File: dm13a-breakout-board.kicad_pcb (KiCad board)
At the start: 2 copper layers, 50 x 50 mm, 11 parts, among them J1 Conn_01x02, J2 Conn_01x05, J3 Conn_01x08, J4 Conn_01x08, U1 DM13A

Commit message: Use different connector, add gnd pins, add silkscreen
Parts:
- J3, J4: value Conn_01x08 -> Conn_02x08_Odd_Even; footprint Connector_PinHeader_2.54mm:PinHeader_1x08_P2.54mm_Vertical -> Connector_PinSocket_2.54mm:PinSocket_2x08_P2.54mm_Vertical
- moved J4 2.50 mm to (89.5, 71.0)
- moved J3 0.55 mm to (63.5, 71.0)
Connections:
- net Net-(J3-Pin_1) renamed /0
- J3 pad 2: Net-(J3-Pin_2) -> GND
- J3 pad 3: Net-(J3-Pin_3) -> /1
- J3 pad 4: Net-(J3-Pin_4) -> GND
- J3 pad 5: Net-(J3-Pin_5) -> /2
- J3 pad 6: Net-(J3-Pin_6) -> GND
- J3 pad 7: Net-(J3-Pin_7) -> /3
- J3 pad 8: Net-(J3-Pin_8) -> GND
- J4 pad 1: Net-(J4-Pin_1) -> GND
- J4 pad 2: Net-(J4-Pin_2) -> /15
- J4 pad 3: Net-(J4-Pin_3) -> GND
- J4 pad 4: Net-(J4-Pin_4) -> /14
- J4 pad 5: Net-(J4-Pin_5) -> GND
- J4 pad 6: Net-(J4-Pin_6) -> /13
- J4 pad 7: Net-(J4-Pin_7) -> GND
- J4 pad 8: Net-(J4-Pin_8) -> /12
- U1 pad 10: Net-(J3-Pin_6) -> /5
- U1 pad 11: Net-(J3-Pin_7) -> /6
- U1 pad 12: Net-(J3-Pin_8) -> /7
- U1 pad 13: Net-(J4-Pin_8) -> /8
- U1 pad 14: Net-(J4-Pin_7) -> /9
- U1 pad 15: Net-(J4-Pin_6) -> /10
- U1 pad 16: Net-(J4-Pin_5) -> /11
- U1 pad 17: Net-(J4-Pin_4) -> /12
- U1 pad 18: Net-(J4-Pin_3) -> /13
- U1 pad 19: Net-(J4-Pin_2) -> /14
- U1 pad 20: Net-(J4-Pin_1) -> /15
- U1 pad 6: Net-(J3-Pin_2) -> /1
- U1 pad 7: Net-(J3-Pin_3) -> /2
- U1 pad 8: Net-(J3-Pin_4) -> /3
- U1 pad 9: Net-(J3-Pin_5) -> /4
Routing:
- net Net-(J4-Pin_2): track 8.53 -> 0.00 mm
- net /14: track 0.00 -> 8.53 mm
- net Net-(J4-Pin_8): track 8.53 -> 0.00 mm
- net Net-(J4-Pin_7): track 8.53 -> 0.00 mm
- net Net-(J4-Pin_6): track 8.53 -> 0.00 mm
- net Net-(J4-Pin_5): track 8.53 -> 0.00 mm
- net Net-(J4-Pin_4): track 8.53 -> 0.00 mm
- net Net-(J4-Pin_3): track 8.53 -> 0.00 mm
- net Net-(J4-Pin_1): track 8.53 -> 0.00 mm
- net /9: track 0.00 -> 8.53 mm
- net /8: track 0.00 -> 8.53 mm
- net /15: track 0.00 -> 8.53 mm
- net /13: track 0.00 -> 8.53 mm
- net /12: track 0.00 -> 8.53 mm
- net /11: track 0.00 -> 8.53 mm
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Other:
- board text added: "0"
- board text added: "1"
- board text added: "10"
- board text added: "11"
- board text added: "12"
- board text added: "13"
- board text added: "14"
- board text added: "15"
- board text added: "2"
- board text added: "3"
- board text added: "4"
- board text added: "5"
- board text added: "6"
- board text added: "7"
- board text added: "8"
- board text added: "9"

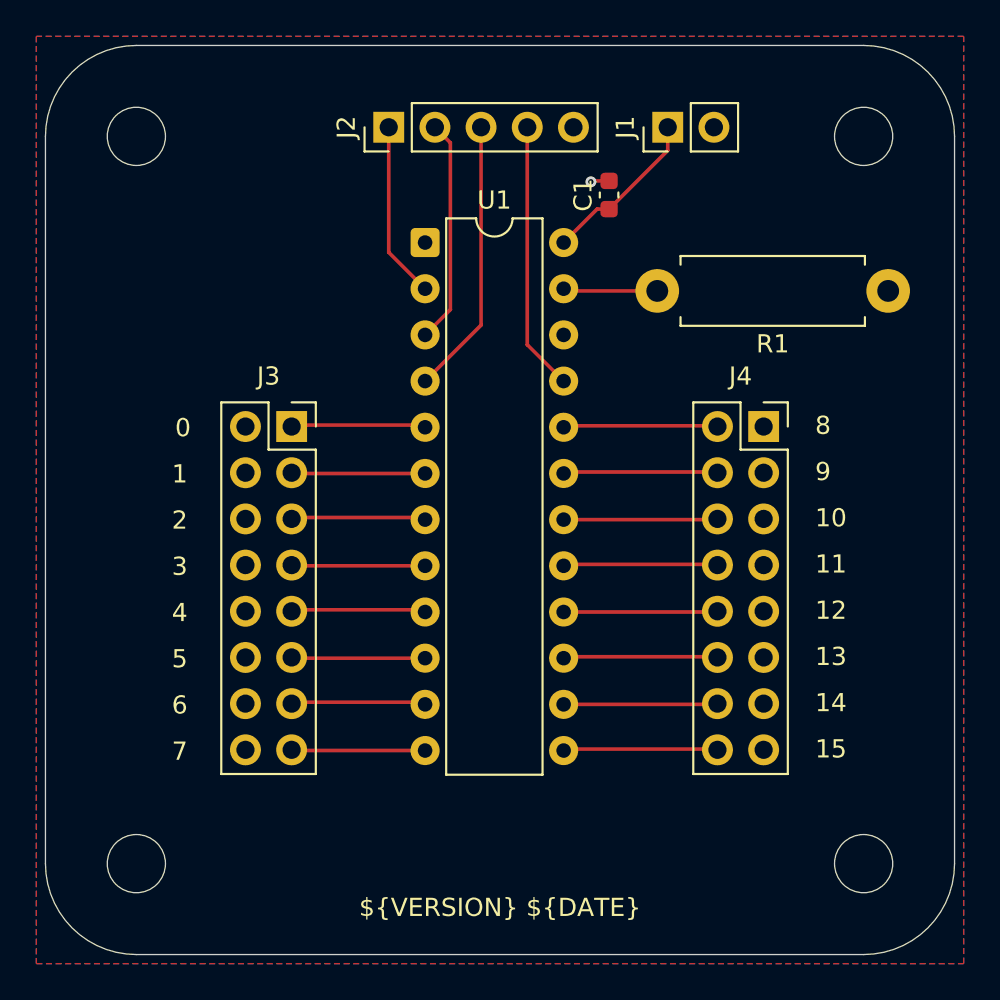
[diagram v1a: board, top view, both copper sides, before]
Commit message: Silkscreen updates (#22)
* Update silkscreen and component placement

* Add note to readme about KiCad git integration
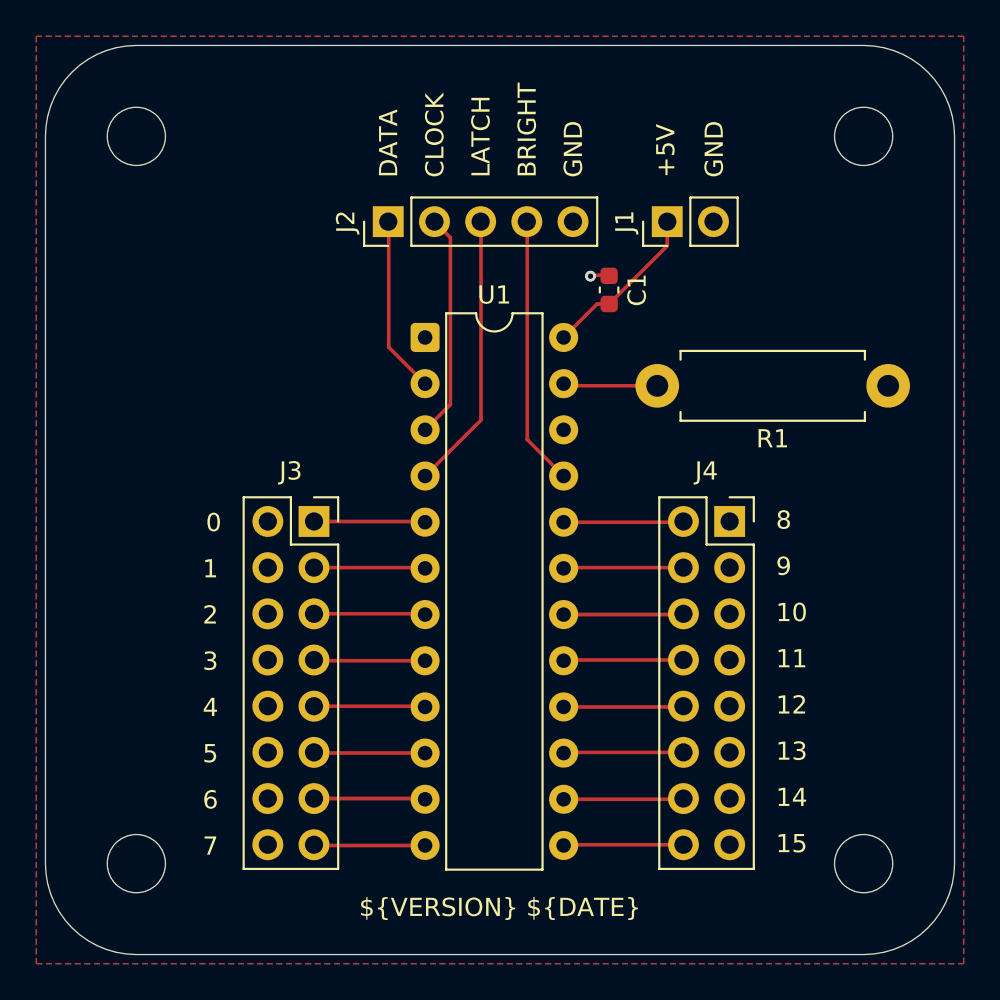
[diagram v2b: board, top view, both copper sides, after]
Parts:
- moved J4 5.55 mm to (87.6, 76.2)
- moved J3 5.36 mm to (64.8, 76.2)
- moved R1 5.22 mm to (96.3, 68.7)
- moved U1 5.22 mm to (70.9, 66.1)
- moved C1 5.22 mm to (81.0, 63.4)
- moved J1 5.19 mm to (84.2, 59.7)
- moved J2 5.19 mm to (68.9, 59.7)
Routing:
- net /9: track 8.53 -> 6.61 mm
- net /13: track 8.53 -> 6.61 mm
- net /11: track 8.53 -> 6.61 mm
- net /14: track 8.53 -> 6.72 mm
- net /12: track 8.53 -> 6.72 mm
- net /8: track 8.53 -> 6.72 mm
- net /10: track 8.53 -> 6.72 mm
- net /3: track 7.93 -> 6.13 mm
- net /1: track 7.93 -> 6.13 mm
- net /7: track 7.93 -> 6.13 mm
- net /5: track 7.93 -> 6.13 mm
- net /6: track 7.93 -> 6.30 mm
- net /2: track 7.93 -> 6.30 mm
- net /0: track 7.93 -> 6.30 mm
- net /4: track 7.93 -> 6.30 mm
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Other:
- board text added: "+5V"
- board text added: "BRIGHT"
- board text added: "CLOCK"
- board text added: "DATA"
- board text added: "GND"
- board text added: "LATCH"
